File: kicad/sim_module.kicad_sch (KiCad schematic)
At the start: 1 part, among them U1 TPD3F303DPVR

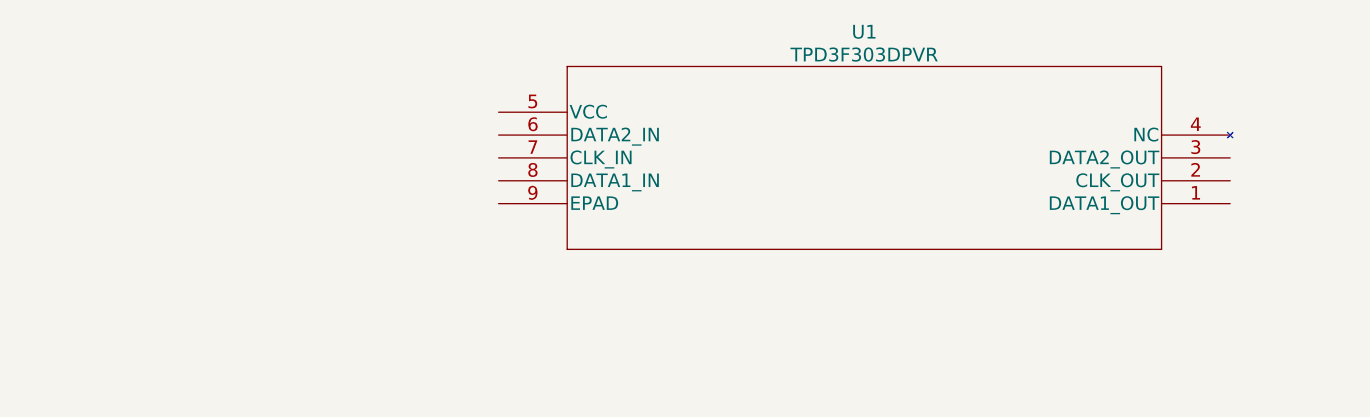
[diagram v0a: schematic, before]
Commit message: Updated nrf9160 symbols for easier use, added sim card holder and doc, added first connections to mcu
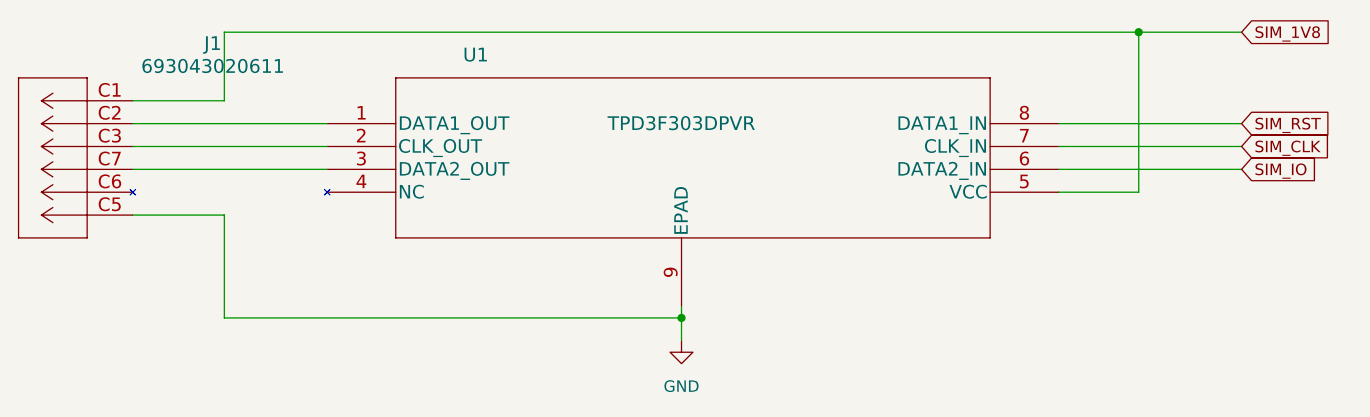
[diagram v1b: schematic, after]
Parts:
- added J1: 693043020611, CONN6_43020611_WRE, symbol 693043020611:693043020611
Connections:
- net at U1.1 (DATA1_OUT): now also J1.C2
- net at U1.2 (CLK_OUT): now also J1.C3
- net at U1.3 (DATA2_OUT): now also J1.C7
- net SIM_1V8: now reaches U1.5 (VCC)
- net SIM_1V8: now also J1.C1
- net SIM_IO: now reaches U1.6 (DATA2_IN)
- net SIM_CLK: now reaches U1.7 (CLK_IN)
- net SIM_RST: now reaches U1.8 (DATA1_IN)
- net GND: now reaches U1.9 (EPAD)
- net GND: now also J1.C5
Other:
- moved on the sheet: U1
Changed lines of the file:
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@@
 (kicad_sch (version 20230121) (generator eeschema)
   (paper "A4")
-  (symbol (lib_id "TPD3F303DPVR:TPD3F303DPVR") (at 212.09 93.98 180) (unit 1)
-    (in_bom yes) (on_board yes) (dnp no) (fields_autoplaced)
-    (property "Reference" "U1" (at 171.45 74.93 0)
+  (junction (at 201.93 74.93) (diameter 0) (color 0 0 0 0)
+  )
+  (junction (at 151.13 106.68) (diameter 0) (color 0 0 0 0)
+  )
+  (wire (pts (xy 100.33 95.25) (xy 100.33 106.68))
+    (stroke (width 0) (type default))
+  )
+  (wire (pts (xy 201.93 74.93) (xy 213.36 74.93))
+    (stroke (width 0) (type default))
+  )
+  (wire (pts (xy 90.17 82.55) (xy 100.33 82.55))
+    (stroke (width 0) (type default))
+  )
+  (wire (pts (xy 193.04 87.63) (xy 213.36 87.63))
+    (stroke (width 0) (type default))
+  )
+  (wire (pts (xy 100.33 74.93) (xy 201.93 74.93))
+    (stroke (width 0) (type default))
+  )
+  (wire (pts (xy 90.17 85.09) (xy 111.76 85.09))
+    (stroke (width 0) (type default))
+  )
+  (wire (pts (xy 193.04 92.71) (xy 201.93 92.71))
+    (stroke (width 0) (type default))
+  )
+  (wire (pts (xy 193.04 85.09) (xy 213.36 85.09))
+    (stroke (width 0) (type default))
+  )
+  (wire (pts (xy 100.33 82.55) (xy 100.33 74.93))
+    (stroke (width 0) (type default))
+  )
+  (wire (pts (xy 90.17 90.17) (xy 111.76 90.17))
+    (stroke (width 0) (type default))
+  )
+  (wire (pts (xy 151.13 105.41) (xy 151.13 106.68))
+    (stroke (width 0) (type default))
+  )
+  (wire (pts (xy 151.13 106.68) (xy 151.13 109.22))
+    (stroke (width 0) (type default))
+  )
+  (wire (pts (xy 90.17 95.25) (xy 100.33 95.25))
+    (stroke (width 0) (type default))
+  )
+  (wire (pts (xy 90.17 87.63) (xy 111.76 87.63))
+    (stroke (width 0) (type default))
+  )
+  (wire (pts (xy 193.04 90.17) (xy 213.36 90.17))
+    (stroke (width 0) (type default))
+  )
+  (wire (pts (xy 201.93 74.93) (xy 201.93 92.71))
+    (stroke (width 0) (type default))
+  )
+  (wire (pts (xy 100.33 106.68) (xy 151.13 106.68))
+    (stroke (width 0) (type default))
+  )
+  (global_label "SIM_1V8" (shape input) (at 213.36 74.93 0) (fields_autoplaced)
+    (effects (font (size 1.27 1.27)) (justify left))
+    (property "Intersheetrefs" "${INTERSHEET_REFS}" (at 224.0067 74.93 0)
+      (effects (font (size 1.27 1.27)) (justify left) hide)
+    )
+  )
+  (global_label "SIM_IO" (shape input) (at 213.36 90.17 0) (fields_autoplaced)
+    (effects (font (size 1.27 1.27)) (justify left))
+    (property "Intersheetrefs" "${INTERSHEET_REFS}" (at 222.4344 90.17 0)
+      (effects (font (size 1.27 1.27)) (justify left) hide)
+    )
+  )
+  (global_label "SIM_CLK" (shape input) (at 213.36 87.63 0) (fields_autoplaced)
+    (effects (font (size 1.27 1.27)) (justify left))
+    (property "Intersheetrefs" "${INTERSHEET_REFS}" (at 224.0672 87.63 0)
+      (effects (font (size 1.27 1.27)) (justify left) hide)
+    )
+  )
+  (global_label "SIM_RST" (shape input) (at 213.36 85.09 0) (fields_autoplaced)
+    (effects (font (size 1.27 1.27)) (justify left))
+    (property "Intersheetrefs" "${INTERSHEET_REFS}" (at 223.9462 85.09 0)
+      (effects (font (size 1.27 1.27)) (justify left) hide)
+    )
+  )
+  (symbol (lib_id "693043020611:693043020611") (at 90.17 82.55 0) (mirror y) (unit 1)
+    (in_bom yes) (on_board yes) (dnp no)
+    (property "Reference" "J1" (at 99.06 76.2 0)
       (effects (font (size 1.524 1.524)))
     )
-    (property "Value" "TPD3F303DPVR" (at 171.45 77.47 0)
+    (property "Value" "693043020611" (at 99.06 78.74 0)
       (effects (font (size 1.524 1.524)))
     )
-    (property "Footprint" "DPV8_1P7X0P4" (at 171.45 100.076 0)
+    (property "Footprint" "CONN6_43020611_WRE" (at 80.01 75.946 0)
       (effects (font (size 1.524 1.524)) hide)
     )
-    (property "Datasheet" "" (at 212.09 93.98 0)
+    (property "Datasheet" "" (at 90.17 82.55 0)
+      (effects (font (size 1.524 1.524)))
+    )
+    (pin "C1")
+    (pin "C2")
+    (pin "C3")
+    (pin "C5")
+    (pin "C6")
+    (pin "C7")
+    (instances
+      (project "IoT_sulari"
+        (path "/184b47ed-2c2b-4c02-be35-d18f4f4e5685/38627e9e-7096-4a1a-bc9e-0f2735fcbe8c"
+          (reference "J1") (unit 1)
+        )
+      )
+    )
+  )
+  (symbol (lib_id "TPD3F303DPVR:TPD3F303DPVR") (at 111.76 85.09 0) (unit 1)
+    (in_bom yes) (on_board yes) (dnp no)
+    (property "Reference" "U1" (at 128.27 77.47 0)
+      (effects (font (size 1.524 1.524)))
+    )
+    (property "Value" "TPD3F303DPVR" (at 151.13 85.09 0)
+      (effects (font (size 1.524 1.524)))
+    )
+    (property "Footprint" "DPV8_1P7X0P4" (at 71.12 91.186 0)
+      (effects (font (size 1.524 1.524)) hide)
+    )
+    (property "Datasheet" "" (at 111.76 85.09 0)
       (effects (font (size 1.524 1.524)))
     )
@@
         )
       )
+    )
+  )
+  (symbol (lib_id "power:GND") (at 151.13 109.22 0) (unit 1)
+    (in_bom yes) (on_board yes) (dnp no) (fields_autoplaced)
+    (property "Reference" "#PWR03" (at 151.13 115.57 0)
+      (effects (font (size 1.27 1.27)) hide)
+    )
+    (property "Value" "GND" (at 151.13 114.3 0)
+      (effects (font (size 1.27 1.27)))
+    )
+    (property "Footprint" "" (at 151.13 109.22 0)
+      (effects (font (size 1.27 1.27)) hide)
+    )
+    (property "Datasheet" "" (at 151.13 109.22 0)
+      (effects (font (size 1.27 1.27)) hide)
+    )
+    (pin "1")
+    (instances
+      (project "IoT_sulari"
+        (path "/184b47ed-2c2b-4c02-be35-d18f4f4e5685/38627e9e-7096-4a1a-bc9e-0f2735fcbe8c"
+          (reference "#PWR03") (unit 1)
+        )
+      )

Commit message: Updated USB module
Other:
- company: (none) -> University of Oulu
- title: (none) -> SIM module
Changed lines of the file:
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@@
 (kicad_sch (version 20230121) (generator eeschema)
   (paper "A4")
+  (title_block
+    (title "SIM module")
+    (date "2023-03-21")
+    (company "University of Oulu")
+    (comment 1 "SIM card holder and ESD protector")
+  )
   (junction (at 201.93 74.93) (diameter 0) (color 0 0 0 0)
   )

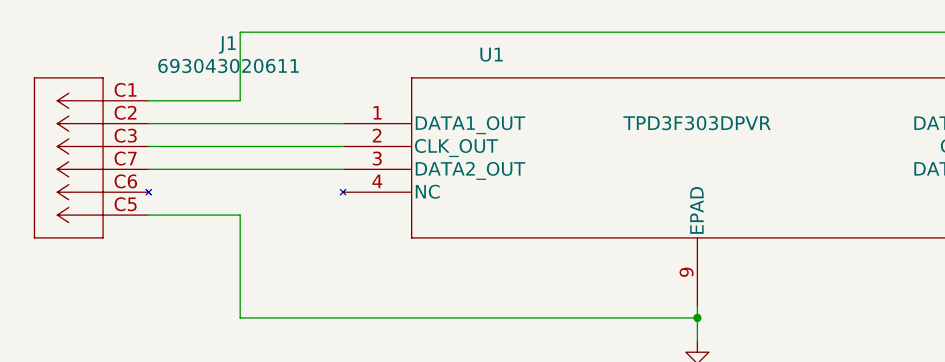
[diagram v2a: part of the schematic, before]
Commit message: added comments and muokkasin komponenttiennumeroinnin selvemmäksi.
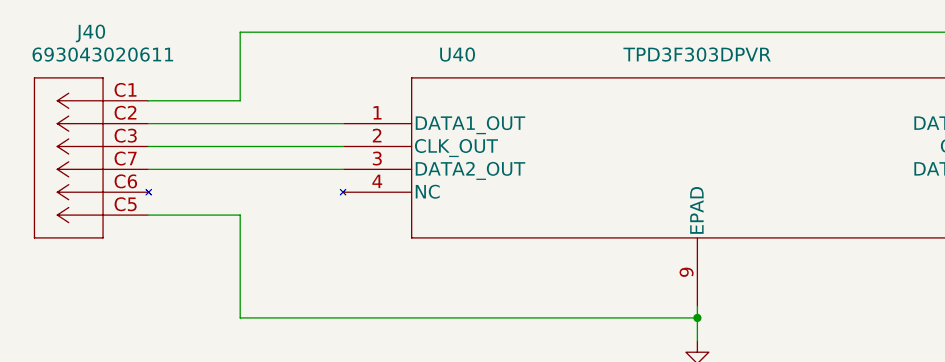
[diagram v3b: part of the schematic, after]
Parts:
- renumbered J1 to J40, U1 to U40
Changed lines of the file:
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@@
   (symbol (lib_id "693043020611:693043020611") (at 90.17 82.55 0) (mirror y) (unit 1)
     (in_bom yes) (on_board yes) (dnp no)
-    (property "Reference" "J1" (at 99.06 76.2 0)
+    (property "Reference" "J40" (at 83.82 74.93 0)
       (effects (font (size 1.524 1.524)))
     )
-    (property "Value" "693043020611" (at 99.06 78.74 0)
+    (property "Value" "693043020611" (at 85.09 77.47 0)
       (effects (font (size 1.524 1.524)))
     )
@@
       (project "IoT_sulari"
         (path "/184b47ed-2c2b-4c02-be35-d18f4f4e5685/38627e9e-7096-4a1a-bc9e-0f2735fcbe8c"
-          (reference "J1") (unit 1)
+          (reference "J40") (unit 1)
         )
       )
@@
   (symbol (lib_id "TPD3F303DPVR:TPD3F303DPVR") (at 111.76 85.09 0) (unit 1)
     (in_bom yes) (on_board yes) (dnp no)
-    (property "Reference" "U1" (at 128.27 77.47 0)
+    (property "Reference" "U40" (at 124.46 77.47 0)
       (effects (font (size 1.524 1.524)))
     )
-    (property "Value" "TPD3F303DPVR" (at 151.13 85.09 0)
+    (property "Value" "TPD3F303DPVR" (at 151.13 77.47 0)
       (effects (font (size 1.524 1.524)))
     )
@@
       (project "IoT_sulari"
         (path "/184b47ed-2c2b-4c02-be35-d18f4f4e5685/38627e9e-7096-4a1a-bc9e-0f2735fcbe8c"
-          (reference "U1") (unit 1)
+          (reference "U40") (unit 1)
         )
       )
